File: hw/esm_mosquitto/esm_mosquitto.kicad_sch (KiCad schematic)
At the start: 21 parts, among them J1 Conn_01x04_Male_Soil_Sensor, J2 Barrel_Jack, U1 ESP-01v090, U2 DHT11, U3 BSS138_4ch, U5 AMS1117-3.3

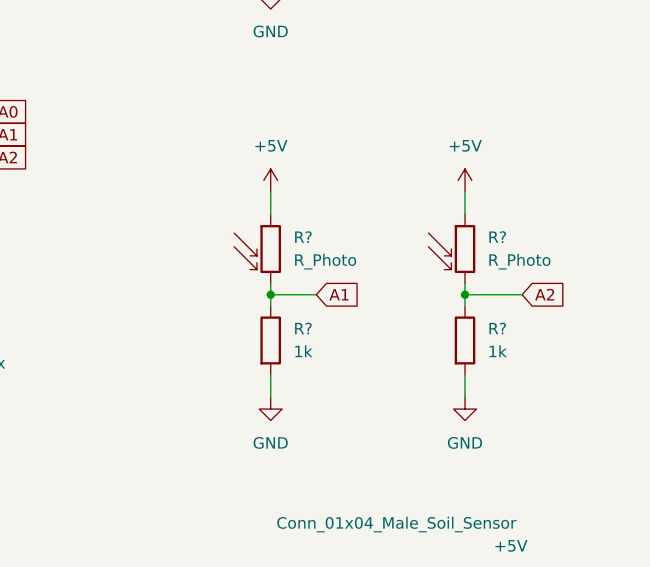
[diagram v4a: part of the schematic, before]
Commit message: - Модифицирован протокол передачи статуса соединения: добавлен уникальный префикс сообщения и циклическая отправка до момента получения подтверждения - Проверена работа передачи статусов 3 и 4 (отключение и подключение MQTT-брокера)
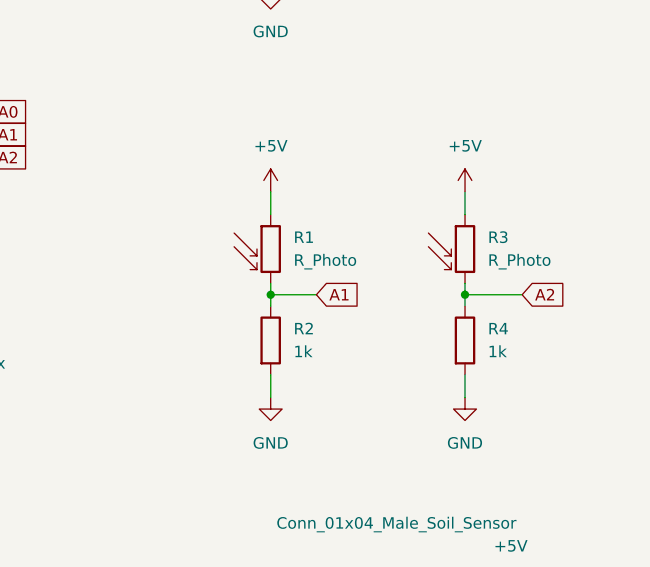
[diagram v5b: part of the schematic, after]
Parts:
- gave numbers to parts that had none: 4
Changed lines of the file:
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@@
   (symbol (lib_id "Device:R") (at 208.28 93.98 0) (unit 1)
     (in_bom yes) (on_board yes) (fields_autoplaced)
-    (property "Reference" "R?" (id 0) (at 210.82 92.7099 0)
+    (property "Reference" "R2" (id 0) (at 210.82 92.7099 0)
       (effects (font (size 1.27 1.27)) (justify left))
     )
@@
   (symbol (lib_id "Device:R_Photo") (at 208.28 83.82 0) (unit 1)
     (in_bom yes) (on_board yes) (fields_autoplaced)
-    (property "Reference" "R?" (id 0) (at 210.82 82.5499 0)
+    (property "Reference" "R1" (id 0) (at 210.82 82.5499 0)
       (effects (font (size 1.27 1.27)) (justify left))
     )
@@
   (symbol (lib_id "Device:R_Photo") (at 229.87 83.82 0) (unit 1)
     (in_bom yes) (on_board yes) (fields_autoplaced)
-    (property "Reference" "R?" (id 0) (at 232.41 82.5499 0)
+    (property "Reference" "R3" (id 0) (at 232.41 82.5499 0)
       (effects (font (size 1.27 1.27)) (justify left))
     )
@@
   (symbol (lib_id "Device:R") (at 229.87 93.98 0) (unit 1)
     (in_bom yes) (on_board yes) (fields_autoplaced)
-    (property "Reference" "R?" (id 0) (at 232.41 92.7099 0)
+    (property "Reference" "R4" (id 0) (at 232.41 92.7099 0)
       (effects (font (size 1.27 1.27)) (justify left))
     )
@@
       (reference "J2") (unit 1) (value "Barrel_Jack") (footprint "TerminalBlock:TerminalBlock_Altech_AK300-2_P5.00mm")
     )
+    (path "/66a63530-21d0-4c46-9871-3b13e24c24f3"
+      (reference "R1") (unit 1) (value "R_Photo") (footprint "Connector_PinHeader_2.54mm:PinHeader_1x02_P2.54mm_Vertical")
+    )
+    (path "/1e3fd3d5-91a2-4915-bf3d-e5e3d46d180b"
+      (reference "R2") (unit 1) (value "1k") (footprint "Resistor_THT:R_Axial_DIN0207_L6.3mm_D2.5mm_P7.62mm_Horizontal")
+    )
+    (path "/7db2a4b9-f872-48cc-a2a7-1f09e20dda1e"
+      (reference "R3") (unit 1) (value "R_Photo") (footprint "Connector_PinHeader_2.54mm:PinHeader_1x02_P2.54mm_Vertical")
+    )
+    (path "/a681347c-2da8-48f2-88a6-f192a29fe2c6"
+      (reference "R4") (unit 1) (value "1k") (footprint "Resistor_THT:R_Axial_DIN0207_L6.3mm_D2.5mm_P7.62mm_Horizontal")
+    )
     (path "/9dcbe3b2-8052-429a-b956-ccd7c975e4f0"
       (reference "R5") (unit 1) (value "10k") (footprint "Resistor_THT:R_Axial_DIN0207_L6.3mm_D2.5mm_P7.62mm_Horizontal")
@@
       (reference "R10") (unit 1) (value "470") (footprint "Resistor_THT:R_Axial_DIN0207_L6.3mm_D2.5mm_P7.62mm_Horizontal")
     )
-    (path "/1e3fd3d5-91a2-4915-bf3d-e5e3d46d180b"
-      (reference "R?") (unit 1) (value "1k") (footprint "Resistor_THT:R_Axial_DIN0207_L6.3mm_D2.5mm_P7.62mm_Horizontal")
-    )
-    (path "/66a63530-21d0-4c46-9871-3b13e24c24f3"
-      (reference "R?") (unit 1) (value "R_Photo") (footprint "Connector_PinHeader_2.54mm:PinHeader_1x02_P2.54mm_Vertical")
-    )
-    (path "/7db2a4b9-f872-48cc-a2a7-1f09e20dda1e"
-      (reference "R?") (unit 1) (value "R_Photo") (footprint "Connector_PinHeader_2.54mm:PinHeader_1x02_P2.54mm_Vertical")
-    )
-    (path "/a681347c-2da8-48f2-88a6-f192a29fe2c6"
-      (reference "R?") (unit 1) (value "1k") (footprint "Resistor_THT:R_Axial_DIN0207_L6.3mm_D2.5mm_P7.62mm_Horizontal")
-    )
     (path "/9826698f-7603-4370-b8fe-754eff05d0c9"
